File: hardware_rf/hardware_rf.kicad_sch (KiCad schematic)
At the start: 92 parts, among them IC1 CC1125RHBR, IC2 BALF-SPI2-02D3, IC3 4259-63, IC4 4259-63, J1 Conn_Coaxial, J2 Conn_01x03_Socket, J3 Conn_02x20_Top_Bottom, J4 USB_C_Receptacle_USB2.0_16P, SW1 SW_Push, U1 RP2350A-QFN60, U2 W25Q128JVS, U3 GSQ5111, U4 SK5129, U5 AMS1117s-3.3, Y1 Crystal_GND24, Y2 Crystal_GND24

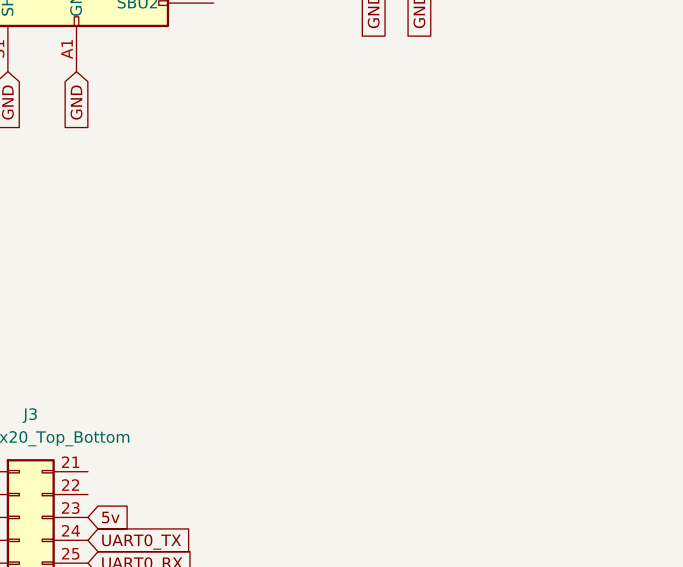
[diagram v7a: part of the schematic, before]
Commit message: added ESD Protection and Moved USB-C Connector pos
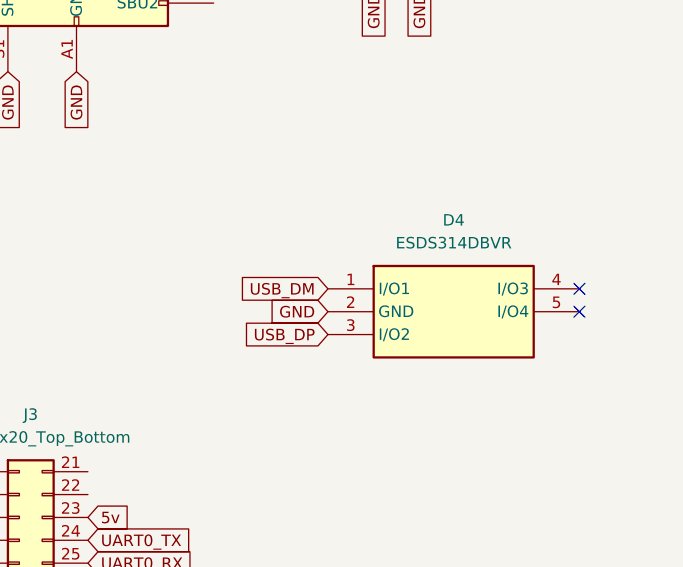
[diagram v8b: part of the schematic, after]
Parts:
- added D4: ESDS314DBVR, user_imported_devices:ESDS314BVR_SOT95P280X145-5N, symbol user_imported:ESDS314DBVR
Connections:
- net GND: now also D4.2 (GND)
- net USB_DM: now also D4.1 (I/O1)
- net USB_DP: now also D4.3 (I/O2)
- no-connect marks 7 -> 9
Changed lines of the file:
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@@
 	)
 	(no_connect
+		(at 383.54 115.57)
+	)
+	(no_connect
 		(at 259.08 149.86)
 	)
@@
 	)
 	(no_connect
+		(at 383.54 118.11)
+	)
+	(no_connect
 		(at 259.08 99.06)
 	)
@@
 		)
 	)
+	(global_label "USB_DM"
+		(shape input)
+		(at 355.6 115.57 180)
+		(fields_autoplaced yes)
+		(effects
+			(font
+				(size 1.27 1.27)
+			)
+			(justify right)
+		)
+		(property "Intersheetrefs" "${INTERSHEET_REFS}"
+			(at 345.1158 115.57 0)
+			(effects
+				(font
+					(size 1.27 1.27)
+				)
+				(justify right)
+				(hide yes)
+			)
+		)
+	)
 	(global_label "QSPI_SD3"
 		(shape input)
@@
 		)
 	)
+	(global_label "GND"
+		(shape input)
+		(at 355.6 118.11 180)
+		(fields_autoplaced yes)
+		(effects
+			(font
+				(size 1.27 1.27)
+			)
+			(justify right)
+		)
+		(property "Intersheetrefs" "${INTERSHEET_REFS}"
+			(at 348.7443 118.11 0)
+			(effects
+				(font
+					(size 1.27 1.27)
+				)
+				(justify right)
+				(hide yes)
+			)
+		)
+	)
 	(global_label "QSPI_SS"
 		(shape input)
@@
 		)
 	)
+	(global_label "USB_DP"
+		(shape input)
+		(at 355.6 120.65 180)
+		(fields_autoplaced yes)
+		(effects
+			(font
+				(size 1.27 1.27)
+			)
+			(justify right)
+		)
+		(property "Intersheetrefs" "${INTERSHEET_REFS}"
+			(at 345.2972 120.65 0)
+			(effects
+				(font
+					(size 1.27 1.27)
+				)
+				(justify right)
+				(hide yes)
+			)
+		)
+	)
 	(global_label "I2C0_SDA"
 		(shape input)
@@
 					(unit 1)
 				)
+			)
+		)
+	)
+	(symbol
+		(lib_id "user_imported:ESDS314DBVR")
+		(at 355.6 115.57 0)
+		(unit 1)
+		(exclude_from_sim no)
+		(in_bom yes)
+		(on_board yes)
+		(dnp no)
+		(fields_autoplaced yes)
+		(property "Reference" "D4"
+			(at 369.57 107.95 0)
+			(effects
+				(font
+					(size 1.27 1.27)
+				)
+			)
+		)
+		(property "Value" "ESDS314DBVR"
+			(at 369.57 110.49 0)
+			(effects
+				(font
+					(size 1.27 1.27)
+				)
+			)
+		)
+		(property "Footprint" "user_imported_devices:ESDS314BVR_SOT95P280X145-5N"
+			(at 379.73 210.49 0)
+			(effects
+				(font
+					(size 1.27 1.27)
+				)
+				(justify left top)
+				(hide yes)
+			)
+		)
+		(property "Datasheet" "http://www.ti.com/lit/gpn/esds314"
+			(at 379.73 310.49 0)
+			(effects
+				(font
+					(size 1.27 1.27)
+				)
+				(justify left top)
+				(hide yes)
+			)
+		)
+		(property "Description" "Data-Line Surge and ESD Protection Diode Array"
+			(at 355.6 115.57 0)
+			(effects
+				(font
+					(size 1.27 1.27)
+				)
+				(hide yes)
+			)
+		)
+		(property "Height" "1.45"
+			(at 379.73 510.49 0)
+			(effects
+				(font
+					(size 1.27 1.27)
+				)
+				(justify left top)
+				(hide yes)
+			)
+		)
+		(property "Mouser Part Number" "595-ESDS314DBVR"
+			(at 379.73 610.49 0)
+			(effects
+				(font
+					(size 1.27 1.27)
+				)
+				(justify left top)
+				(hide yes)
+			)
+		)
+		(property "Mouser Price/Stock" "https://www.mouser.co.uk/ProductDetail/Texas-Instruments/ESDS314DBVR?qs=w%2Fv1CP2dgqpkGBpJKrSLAg%3D%3D"
+			(at 379.73 710.49 0)
+			(effects
+				(font
+					(size 1.27 1.27)
+				)
+				(justify left top)
+				(hide yes)
+			)
+		)
+		(property "Manufacturer_Name" "Texas Instruments"
+			(at 379.73 810.49 0)
+			(effects
+				(font
+					(size 1.27 1.27)
+				)
+				(justify left top)
+				(hide yes)
+			)
+		)
+		(property "Manufacturer_Part_Number" "ESDS314DBVR"
+			(at 379.73 910.49 0)
+			(effects
+				(font
+					(size 1.27 1.27)
+				)
+				(justify left top)
+				(hide yes)
+			)
+		)
+		(pin "4"
+		)
+		(pin "5"
+		)
+		(pin "1"
+		)
+		(pin "2"
+		)
+		(pin "3"
+		)
+		(instances
+			(project ""
+				(path "/76e9da14-bca7-4795-80b8-b5efcf73ac31"
+					(reference "D4")
+					(unit 1)
+				)
